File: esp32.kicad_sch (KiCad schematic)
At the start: 14 parts, among them J2 Conn_01x05_Pin, Q3 MMBT3904, Q4 MMBT3904, Y1 ECS-2520MV-xxx-xx

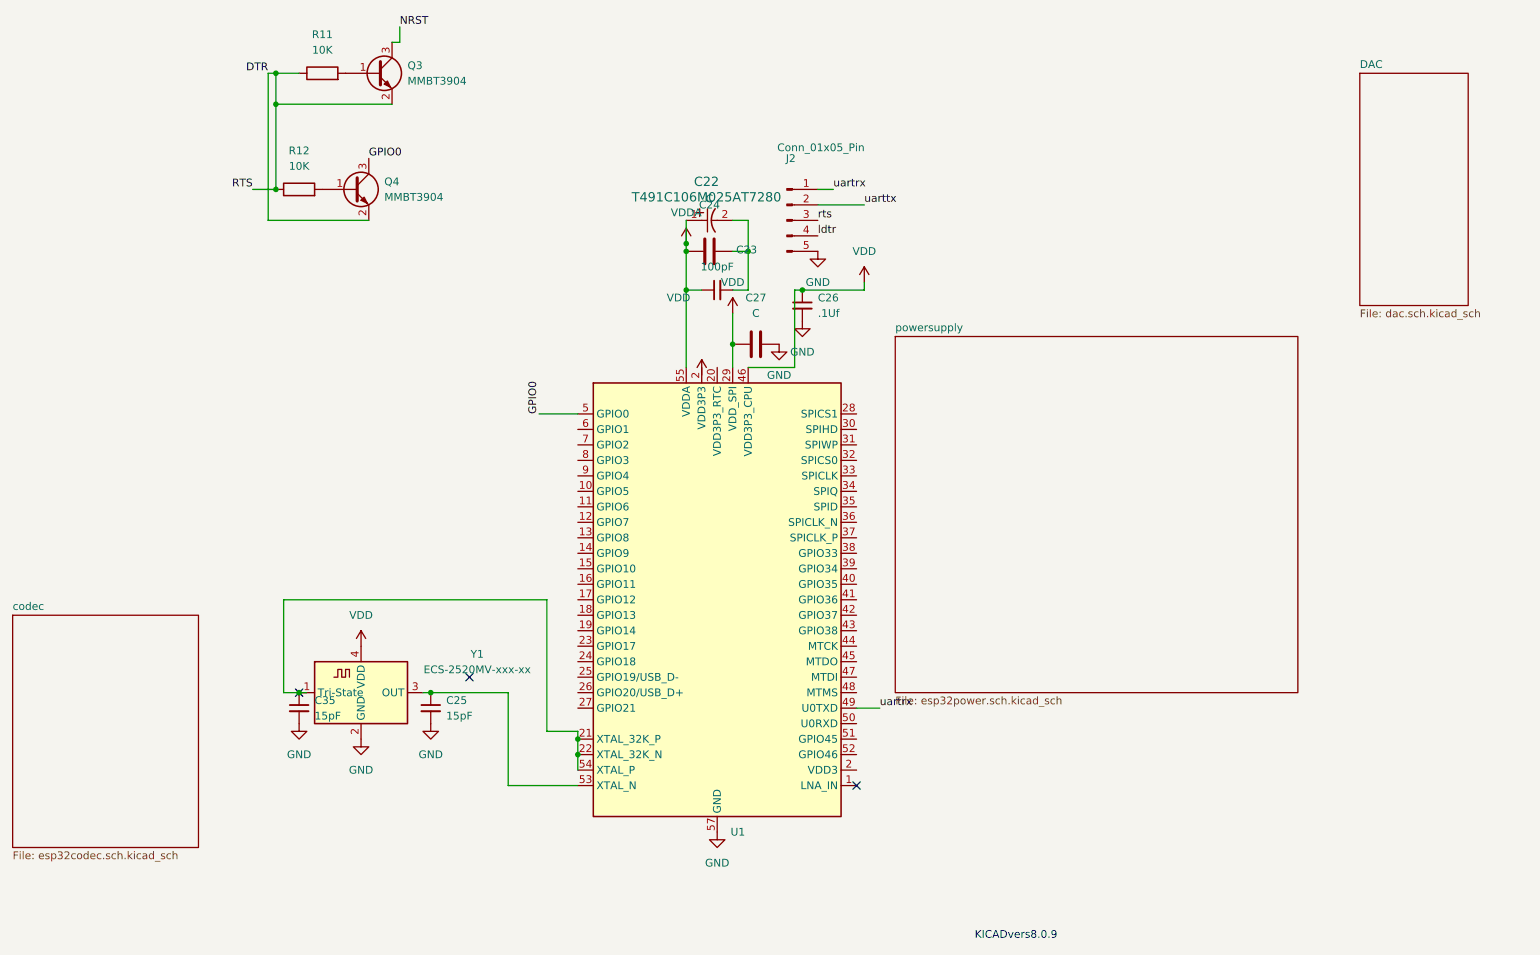
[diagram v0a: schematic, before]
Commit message: updated common lib symbols and footprint models
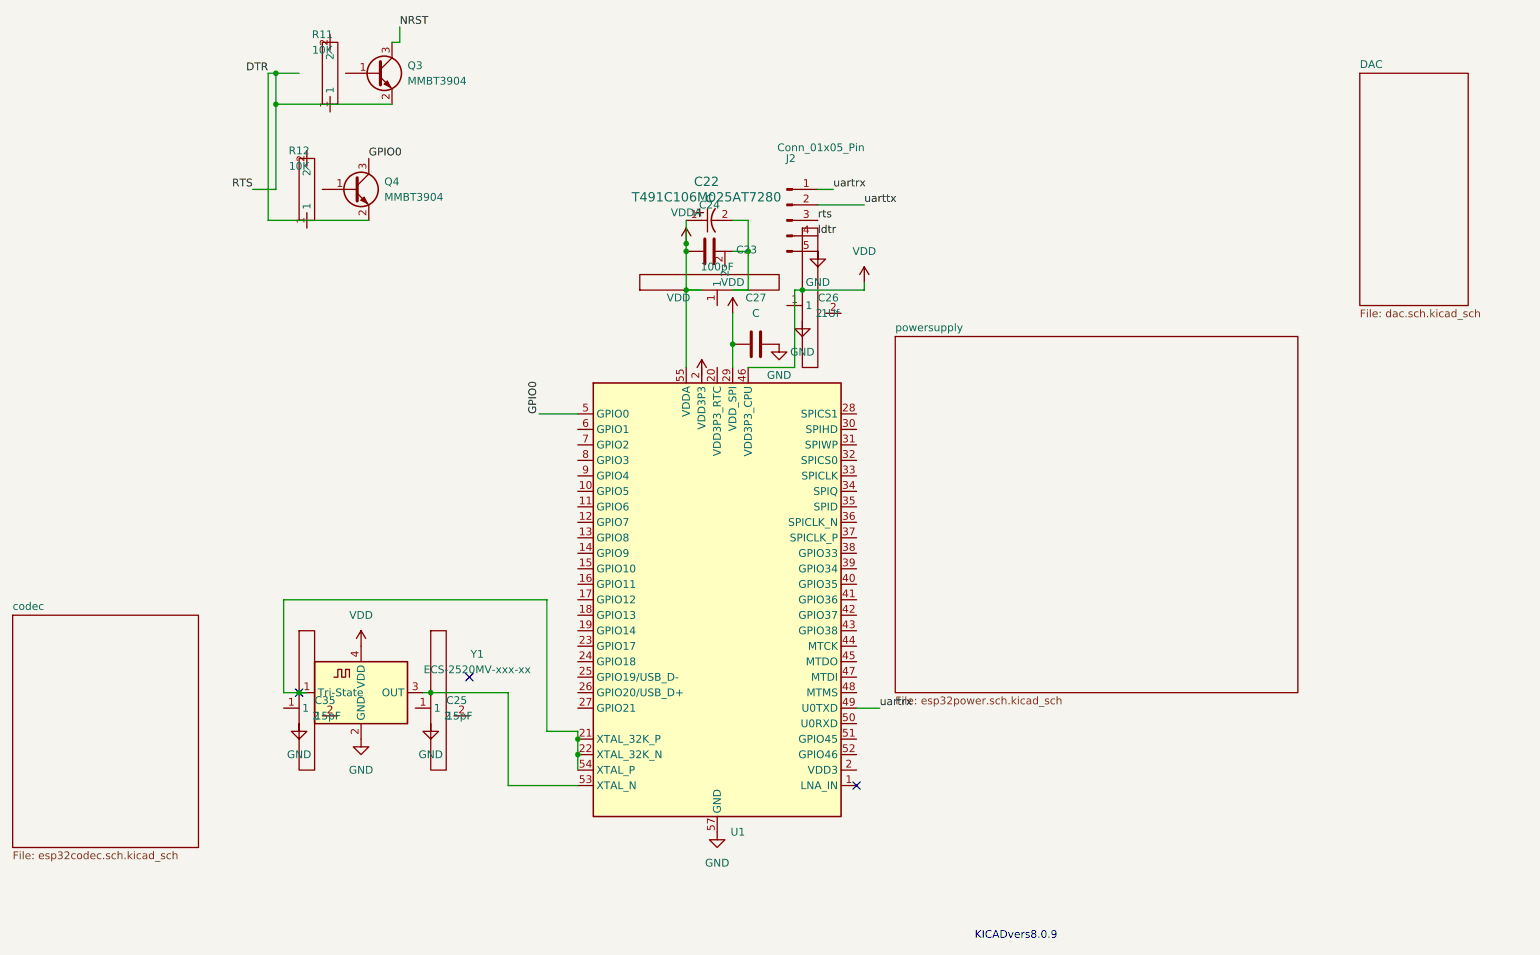
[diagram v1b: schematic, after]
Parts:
- C23: footprint (none) -> commonfootprint:Ceramic0603; symbol Device:C_Small -> common:CerCap
- C25, C26, C35: footprint Capacitor_SMD:C_0201_0603Metric -> commonfootprint:Ceramic0603; symbol Device:C_Small -> common:CerCap
- R11, R12: footprint (none) -> commonfootprint:Modcan0603; symbol Device:R -> common:R
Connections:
- net DTR: no longer R11.1, R12.1
- net GND: no longer C25.2, C26.2, C35.2
- net VDD: no longer C26.1
- net VDDA: no longer C23.1
- net at U1.2 (VDD3P3): now also U1.3 (VDD3P3)
- net at U1.21 (XTAL_32K_P), U1.22 (XTAL_32K_N), U1.54 (XTAL_P)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: no longer C35.1
- net at U1.53 (XTAL_N), Y1.3 (OUT): no longer C25.1
- net at C22.2, C24.2: no longer C23.2
- net at R11.2: no longer Q3.1 (B)
- net at R12.2: no longer Q4.1 (B)
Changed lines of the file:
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@@
-		(color 0 0 0 0)
-	)
-	(junction
-		(at 66.04 49.53)
-		(diameter 0)
 		(color 0 0 0 0)
 	)
@@
 	)
 	(symbol
-		(lib_id "Device:C_Small")
+		(lib_id "common:CerCap")
 		(at 138.43 66.04 90)
 		(unit 1)
@@
 			)
 		)
-		(property "Footprint" ""
+		(property "Footprint" "commonfootprint:Ceramic0603"
 			(at 138.43 66.04 0)
 			(effects
@@
 	)
 	(symbol
-		(lib_id "Device:R")
+		(lib_id "common:R")
 		(at 73.66 30.48 90)
 		(unit 1)
@@
 			)
 		)
-		(property "Footprint" ""
+		(property "Footprint" "commonfootprint:Modcan0603"
 			(at 73.66 32.258 90)
 			(effects
@@
 	)
 	(symbol
-		(lib_id "Device:R")
+		(lib_id "common:R")
 		(at 69.85 49.53 90)
 		(unit 1)
@@
 			)
 		)
-		(property "Footprint" ""
+		(property "Footprint" "commonfootprint:Modcan0603"
 			(at 69.85 51.308 90)
 			(effects
@@
 	)
 	(symbol
-		(lib_id "Device:C_Small")
+		(lib_id "common:CerCap")
 		(at 69.85 134.62 0)
 		(unit 1)
@@
 			)
 		)
-		(property "Footprint" "Capacitor_SMD:C_0201_0603Metric"
+		(property "Footprint" "commonfootprint:Ceramic0603"
 			(at 69.85 134.62 0)
 			(effects
@@
 	)
 	(symbol
-		(lib_id "Device:C_Small")
+		(lib_id "common:CerCap")
 		(at 152.4 68.58 0)
 		(unit 1)
@@
 			)
 		)
-		(property "Footprint" "Capacitor_SMD:C_0201_0603Metric"
+		(property "Footprint" "commonfootprint:Ceramic0603"
 			(at 152.4 68.58 0)
 			(effects
@@
 	)
 	(symbol
-		(lib_id "Device:C_Small")
+		(lib_id "common:CerCap")
 		(at 91.44 134.62 0)
 		(unit 1)
@@
 			)
 		)
-		(property "Footprint" "Capacitor_SMD:C_0201_0603Metric"
+		(property "Footprint" "commonfootprint:Ceramic0603"
 			(at 91.44 134.62 0)
 			(effects

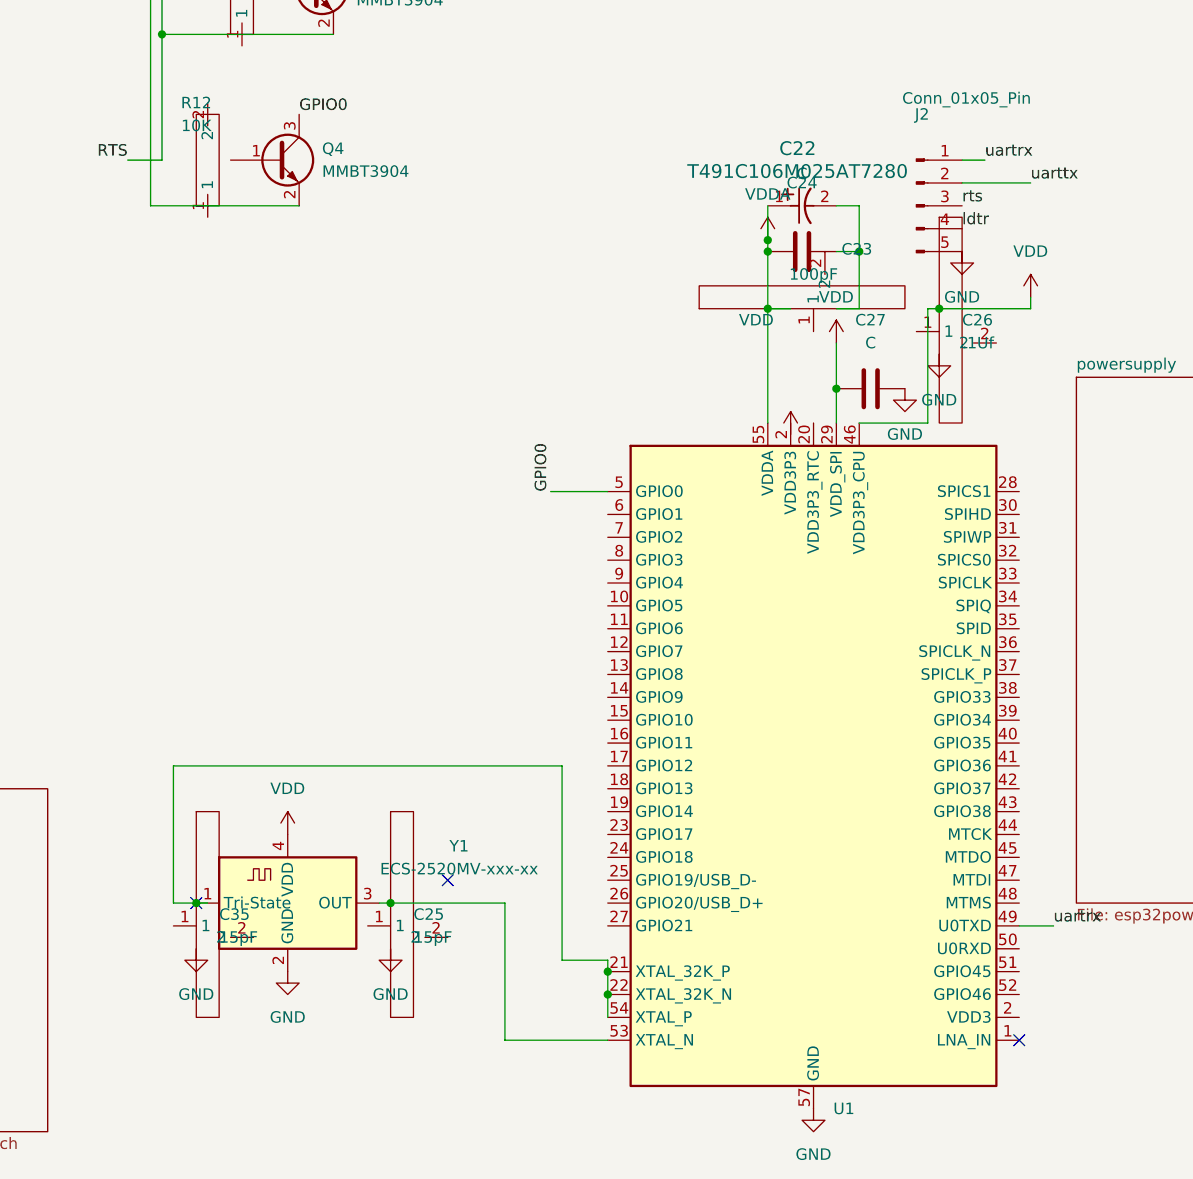
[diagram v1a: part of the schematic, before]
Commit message: updated a few caps
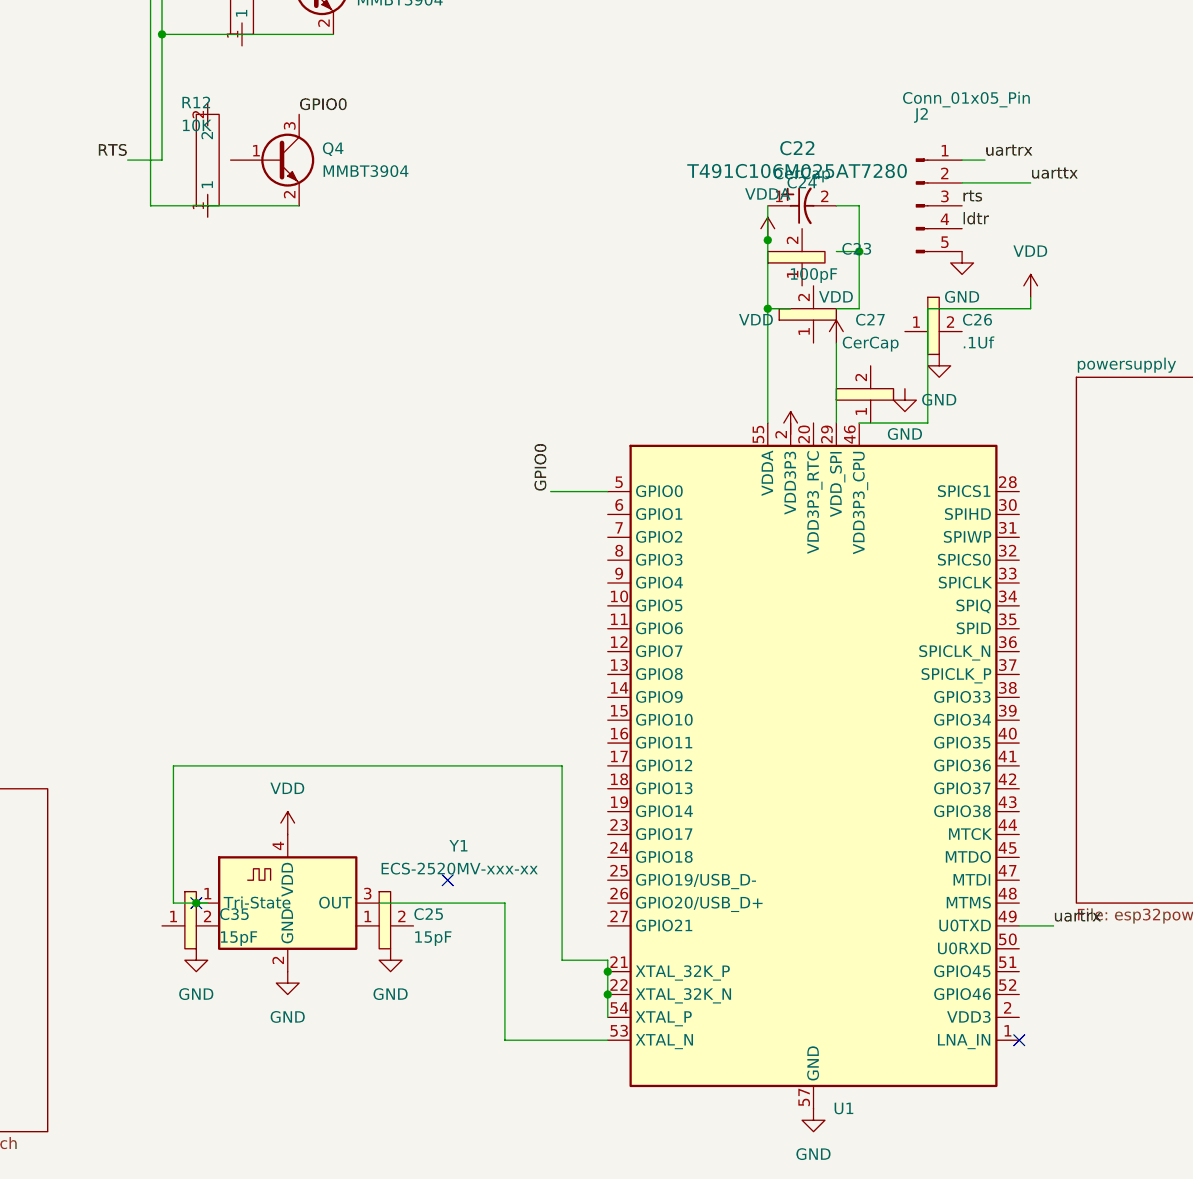
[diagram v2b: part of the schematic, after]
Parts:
- C24, C27: value C -> CerCap; footprint (none) -> commonfootprint:Ceramic0603; symbol Device:C -> common:CerCap
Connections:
- net GND: no longer C27.2
- net VDD: no longer C27.1
- net VDDA: no longer C24.1
- net at U1.2 (VDD3P3): now also U1.3 (VDD3P3)
- net at C22.2: no longer C24.2
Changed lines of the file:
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@@
-	)
-	(junction
-		(at 152.4 66.04)
-		(diameter 0)
-		(color 0 0 0 0)
 	)
 	(junction
@@
 	)
 	(junction
-		(at 133.35 59.69)
-		(diameter 0)
-		(color 0 0 0 0)
-	)
-	(junction
 		(at 66.04 35.56)
 		(diameter 0)
@@
 	)
 	(junction
-		(at 140.97 74.93)
-		(diameter 0)
-		(color 0 0 0 0)
-	)
-	(junction
 		(at 115.57 142.24)
 		(diameter 0)
@@
 		(color 0 0 0 0)
 	)
-	(junction
-		(at 91.44 132.08)
-		(diameter 0)
-		(color 0 0 0 0)
-	)
 	(no_connect
 		(at 97.79 129.54)
@@
 	(wire
 		(pts
-			(xy 133.35 59.69) (xy 133.35 66.04)
-		)
-		(stroke
-			(width 0)
-			(type default)
-		)
-	)
-	(wire
-		(pts
 			(xy 143.51 54.61) (xy 143.51 59.69)
 		)
@@
 	(wire
 		(pts
-			(xy 91.44 132.08) (xy 104.14 132.08)
-		)
-		(stroke
-			(width 0)
-			(type default)
-		)
-	)
-	(wire
-		(pts
 			(xy 109.22 86.36) (xy 115.57 86.36)
 		)
@@
 	(wire
 		(pts
-			(xy 91.44 132.08) (xy 90.17 132.08)
+			(xy 90.17 132.08) (xy 104.14 132.08)
 		)
 		(stroke
@@
 	(wire
 		(pts
-			(xy 140.97 69.85) (xy 140.97 74.93)
+			(xy 140.97 69.85) (xy 140.97 78.74)
 		)
 		(stroke
@@
 	(wire
 		(pts
-			(xy 133.35 58.42) (xy 133.35 59.69)
+			(xy 133.35 58.42) (xy 133.35 66.04)
 		)
 		(stroke
@@
 	(wire
 		(pts
-			(xy 152.4 66.04) (xy 151.13 66.04)
+			(xy 151.13 66.04) (xy 162.56 66.04)
 		)
 		(stroke
@@
 	(wire
 		(pts
-			(xy 162.56 66.04) (xy 152.4 66.04)
-		)
-		(stroke
-			(width 0)
-			(type default)
-		)
-	)
-	(wire
-		(pts
 			(xy 151.13 78.74) (xy 143.51 78.74)
 		)
@@
 		(pts
 			(xy 115.57 139.7) (xy 115.57 138.43)
-		)
-		(stroke
-			(width 0)
-			(type default)
-		)
-	)
-	(wire
-		(pts
-			(xy 140.97 74.93) (xy 140.97 78.74)
 		)
 		(stroke
@@
 	)
 	(symbol
-		(lib_id "Device:C")
+		(lib_id "common:CerCap")
 		(at 137.16 59.69 90)
 		(unit 1)
@@
 			)
 		)
-		(property "Value" "C"
+		(property "Value" "CerCap"
 			(at 137.16 51.054 90)
 			(effects
@@
 			)
 		)
-		(property "Footprint" ""
+		(property "Footprint" "commonfootprint:Ceramic0603"
 			(at 140.97 58.7248 0)
 			(effects
@@
 	)
 	(symbol
-		(lib_id "Device:C")
+		(lib_id "common:CerCap")
 		(at 144.78 74.93 90)
 		(unit 1)
@@
 			)
 		)
-		(property "Value" "C"
+		(property "Value" "CerCap"
 			(at 144.78 69.85 90)
 			(effects
@@
 			)
 		)
-		(property "Footprint" ""
+		(property "Footprint" "commonfootprint:Ceramic0603"
 			(at 148.59 73.9648 0)
 			(effects
